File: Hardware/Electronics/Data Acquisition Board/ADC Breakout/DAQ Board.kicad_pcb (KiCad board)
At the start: 2 copper layers, 50 x 42.7 mm, 59 parts, among them J1 Conn_01x16, J2 Conn_01x16, U1 MCP1755T-5002E_SOT223-5, U2 LM3480-3.3

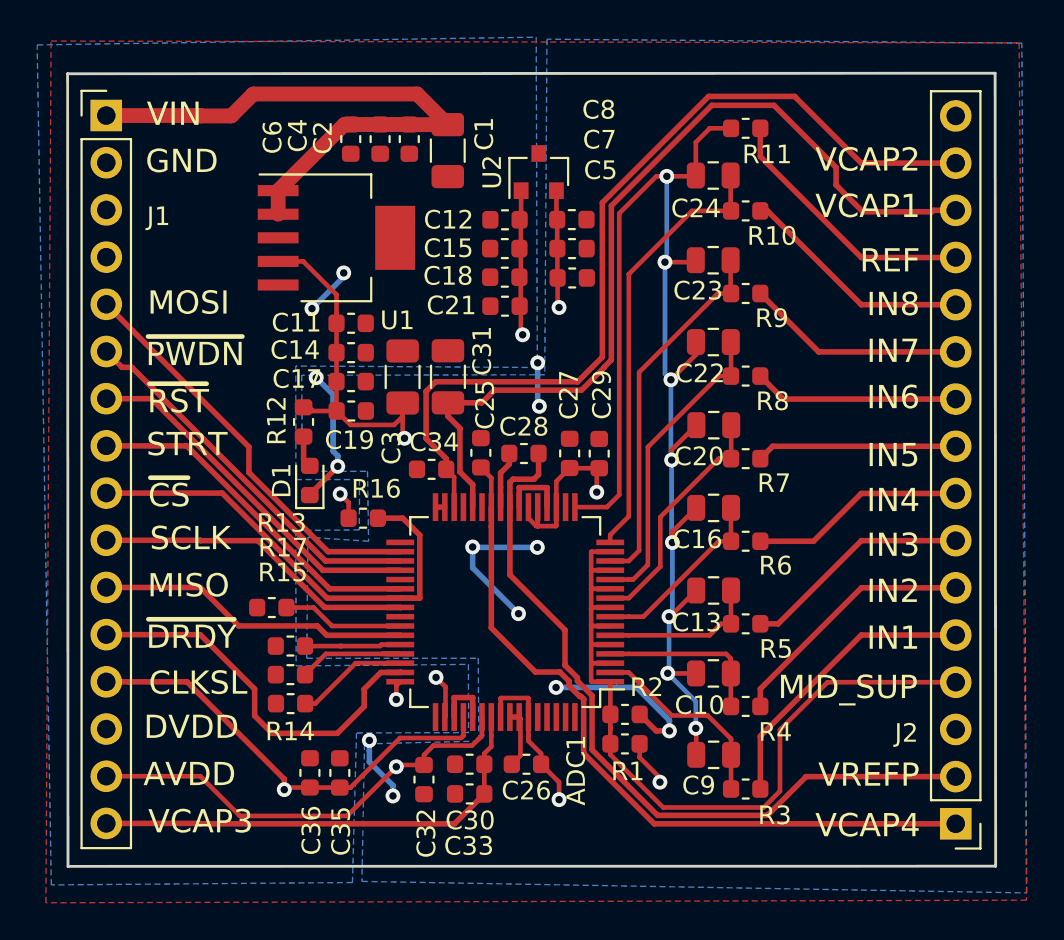
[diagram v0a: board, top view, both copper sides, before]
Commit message: Changed unused analog inputs to AVDD, removed mid supply voltage divider. Small routing change
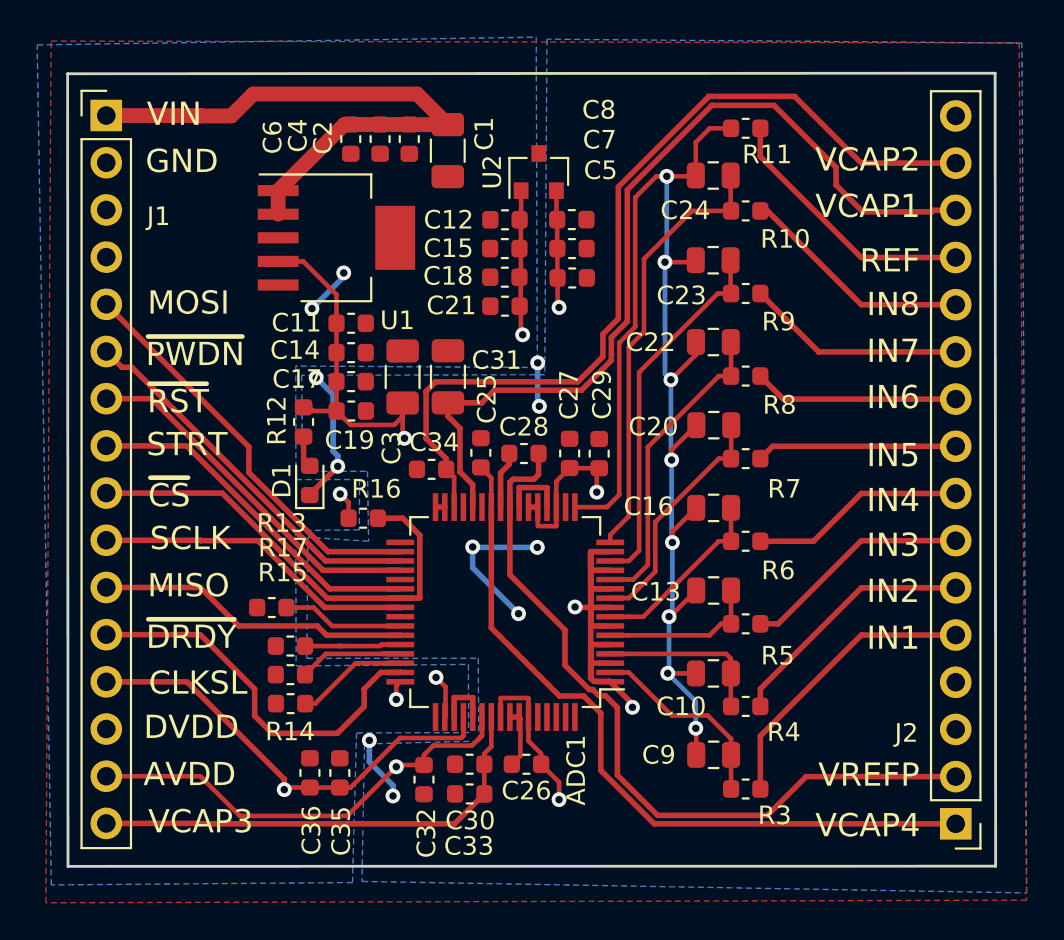
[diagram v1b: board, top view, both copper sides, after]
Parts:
- removed R1, R2: 10k, Resistor_SMD:R_0603_1608Metric
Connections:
- ADC1 pad 1: /MID_SUPPLY -> /AVDD
- ADC1 pad 11: /MID_SUPPLY -> /AVDD
- ADC1 pad 13: /MID_SUPPLY -> /AVDD
- ADC1 pad 15: /MID_SUPPLY -> /AVDD
- ADC1 pad 3: /MID_SUPPLY -> /AVDD
- ADC1 pad 5: /MID_SUPPLY -> /AVDD
- ADC1 pad 7: /MID_SUPPLY -> /AVDD
- ADC1 pad 9: /MID_SUPPLY -> /AVDD
- J2 pad 4: /MID_SUPPLY -> Net-(J2-Pad4)
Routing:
- net /MID_SUPPLY: track 43.8 -> 0.00 mm
- net /AVDD: track 71.0 -> 96.6 mm, vias 6 -> 7
- net /AVSS: track 46.9 -> 37.6 mm, vias 13 -> 11
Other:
- board text removed: "MID_SUP"

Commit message: Small clearance changes, silkscreen art added
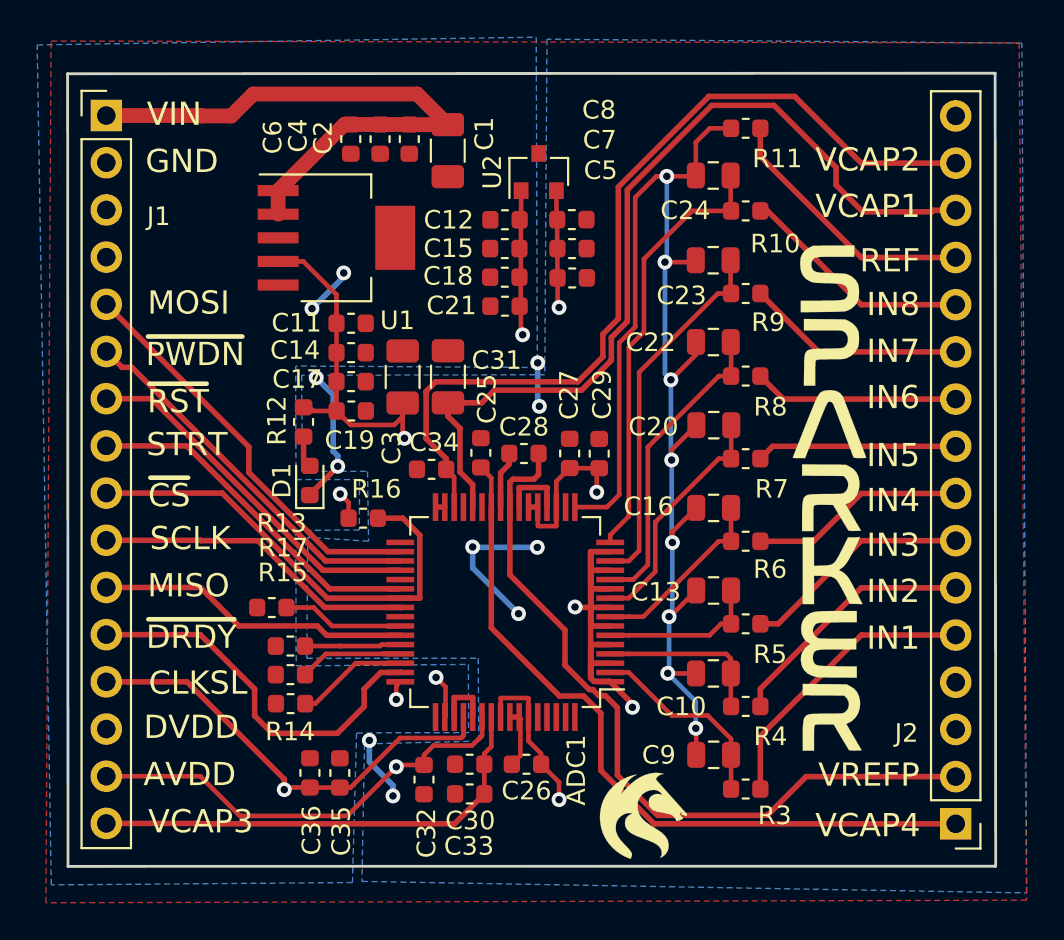
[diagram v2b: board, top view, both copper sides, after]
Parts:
- added G***: LOGO, Sparker:UoN_Small, F.Cu at (107.6, 119.0)
- added G***: LOGO, Sparker:NASA_Vertical, F.Cu at (117.7, 101.8)

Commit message: Removed pullup resistor on /CS. Reran production pdfs and plotted schematic
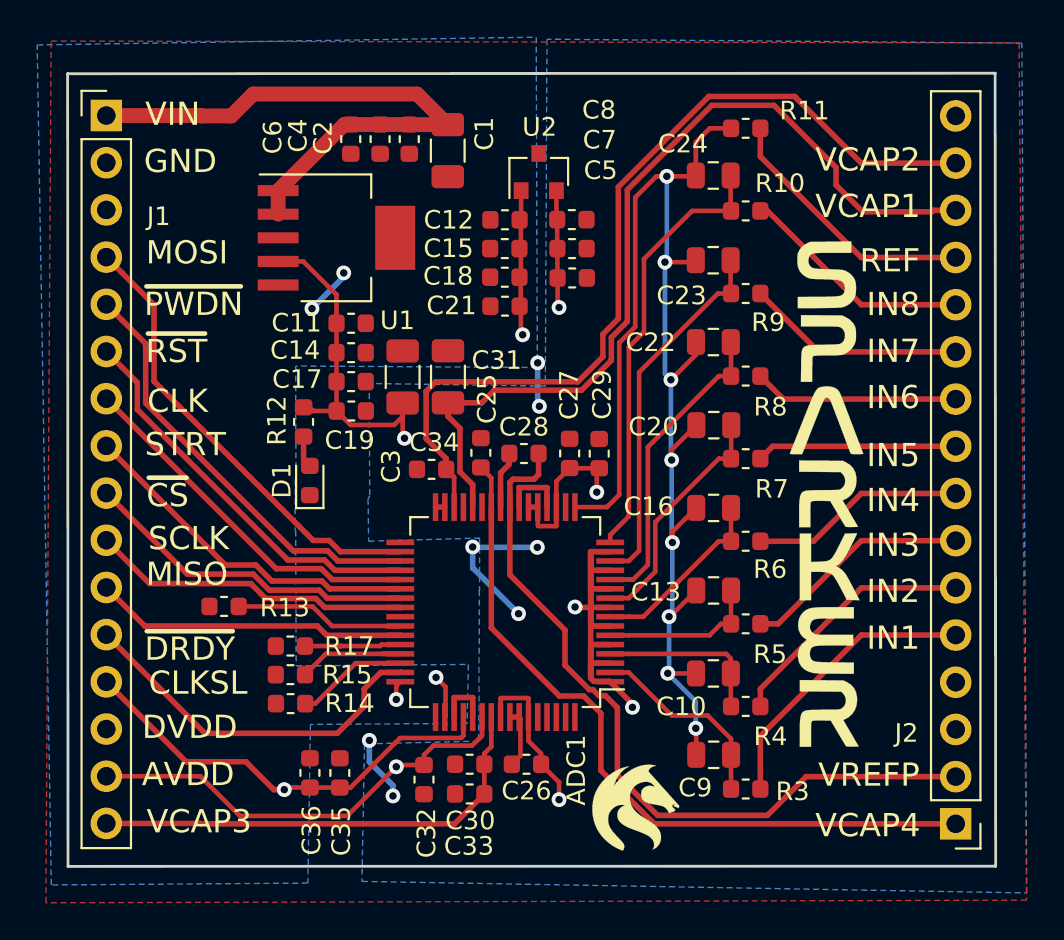
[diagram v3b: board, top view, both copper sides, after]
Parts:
- removed R16: 100k, Resistor_SMD:R_0603_1608Metric
- moved R13 2.57 mm to (85.1, 107.7)
- moved G*** 0.60 mm to (107.2, 118.5)
- moved G*** 0.26 mm to (117.5, 101.6)
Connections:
- ADC1 pad 37: Net-(ADC1-Pad37) -> /CLK
- J1 pad 4: Net-(J1-Pad4) -> /MOSI
- J1 pad 5: /MOSI -> /~PWDN
- J1 pad 6: /~PWDN -> /~RESET
- J1 pad 7: /~RESET -> /CLK
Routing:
- net /CLK: track 0.00 -> 19.9 mm
- net /AVSS: track 37.6 -> 30.2 mm, vias 11 -> 9
- net /~CS: track 25.2 -> 18.2 mm
- net /~PWDN: track 20.5 -> 23.4 mm
- net /MOSI: track 22.1 -> 24.8 mm
- net Net-(ADC1-Pad42): track 7.07 -> 9.13 mm
- net /~RESET: track 19.6 -> 21.6 mm
- net /DVDD: track 37.0 -> 35.2 mm, vias 5 -> 4
- net /~DRDY: track 20.8 -> 20.0 mm
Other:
- rule trace_min: 0.2 -> 0.21
- board text added: "CLK"

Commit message: Small routing change, added extra silkscreen labels
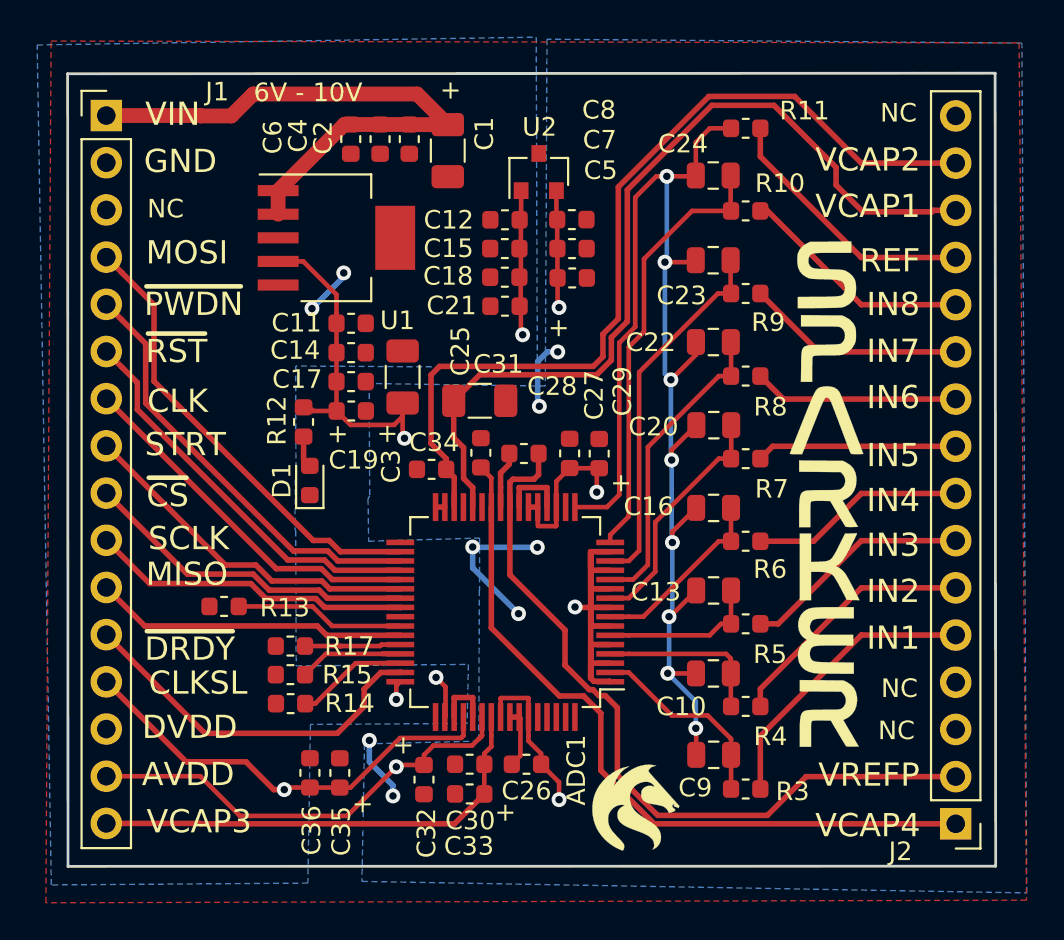
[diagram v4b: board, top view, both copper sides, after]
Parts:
- moved C31 2.14 mm to (98.8, 96.6), turned to 0 degrees
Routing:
- net /AVDD: track 96.6 -> 94.8 mm, vias 7 -> 6
- net /AVSS: track 30.2 -> 31.6 mm
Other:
- board text added: "+"
- board text added: "6V - 10V"
- board text added: "NC"
